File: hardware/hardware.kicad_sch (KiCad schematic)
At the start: 74 parts, among them J1 5025700893, J2 SMA, SW1 PWR switch, U1 BME280, U2 ADS1115IDGS, U3 MS5611-01BA, U4 NEO-M9N, U5 LM2596T-3.3, U6 CC1101RGPR, U7 CC1190RGVT, U8 B39921B3588U410, Y1 26.0 Mhz

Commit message: Updated schematic with better design practices.
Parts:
- removed AE1: W3011, W3011:XDCR_W3011, symbol W3011:W3011
- removed B1: 1079, 1079_KEY, symbol 2026-07-24_00-32-24:1079
- removed C1: 680 uF, symbol Device:C_US
- removed C10, C9: 100pF +- 5%, symbol Device:C_US
- removed C11: 1pF5 +- 0.25%, symbol Device:C_US
- removed C12: 47pF +- 5%, symbol Device:C_US
- removed C13: 0.8pF +- 0.1pF, symbol Device:C_US
- removed C14, C15, C16, C17, C18, C19, C3, C6, C7: 100nF +- 10%, symbol Device:C_US
- removed C2: 330/35 uF/V, symbol Device:C_US
- removed C20: 220 uF, symbol Device:C_US
- removed C21: 10 uF, symbol Device:C_US
- removed C22: 15 pF, symbol Device:C_US
- removed C23: 27 pF, symbol Device:C_US
- removed C24: 1 uF, symbol Device:C_US
- removed C25, C27: 47 pF, symbol Device:C_US
- removed C26: 1 nF, symbol Device:C_US
- removed C28, C29: 12 pF, symbol Device:C_US
- removed C30: 3.3 pF, symbol Device:C_US
- removed C31: 7.5 pF, symbol Device:C_US
- removed C32: DNP, symbol Device:C_US
- removed C33: 1uF, symbol Device:C_US
- removed C4: 12pF +- 5%, symbol Device:C_US
- removed C5: 15pF +- 5%, symbol Device:C_US
- removed C8: 1pF +- .25%, symbol Device:C_US
- removed D0: Red, symbol Device:LED
- removed D1: Blue, symbol Device:LED
- removed D2: 1N5820, Diode_THT:D_DO-201AD_P15.24mm_Horizontal, symbol Diode:1N5820
- removed J1: 5025700893, 502570-0893_MOL, symbol 2026-07-24_01-58-48:5025700893
- removed J2: SMA, symbol Connector:Conn_Coaxial_Small
- removed L10: 7.5 nF, symbol Device:L
- removed L11: 2.9 nF, symbol Device:L
- removed L12: 9.1 nF, symbol Device:L
- removed L13: Bead, symbol Device:L
- removed L3: 12nH +- 5%, symbol Device:L
- removed L4: 18nH +-5%, symbol Device:L
- removed L5: 18nH +- 5&, symbol Device:L
- removed L6: 10nH +-2%, symbol Device:L
- removed L7: 11nH, symbol Device:L
- removed L8: 1.5nH, symbol Device:L
- removed L9: 22nH, symbol Device:L
- removed R1: 10K, symbol Device:R_US
- removed R2, R3: 330, symbol Device:R_US
- removed R4, R5: 33, symbol Device:R_US
- removed R6: 56K, symbol Device:R_US
- removed R7: 3.3K, symbol Device:R_US
- removed R8: 47, symbol Device:R_US
- removed R9: 10, symbol Device:R_US
- removed RT1: PPG102JA, symbol PPG102JA:PPG102JA
- removed SW1: PWR switch, symbol Switch:SW_SPST
- removed U1: BME280, Package_LGA:Bosch_LGA-8_2.5x2.5mm_P0.65mm_ClockwisePinNumbering, symbol Sensor:BME280
- removed U2: ADS1115IDGS, Package_SO:TSSOP-10_3x3mm_P0.5mm, symbol Analog_ADC:ADS1115IDGS
- removed U3: MS5611-01BA, Package_LGA:LGA-8_3x5mm_P1.25mm, symbol Sensor_Pressure:MS5611-01BA
- removed U4: NEO-M9N, RF_GPS:ublox_NEO, symbol RF_GPS:NEO-M9N
- removed U5: LM2596T-3.3, Package_TO_SOT_SMD:TO-263-5_TabPin3, symbol Regulator_Switching:LM2596T-3.3
- removed U6: CC1101RGPR, RGP20_2P4X2P4, symbol 2026-06-04_15-53-20:CC1101RGPR
- removed U7: CC1190RGVT, RGV0016A, symbol 2026-07-24_18-45-18:CC1190RGVT
- removed U8: B39921B3588U410, B39162B3522U410_TDK, symbol 2026-07-24_18-58-53:B39921B3588U410
- removed Y1: 26.0 Mhz, symbol Device:Crystal
- added C1, C30: 1uF, symbol Device:C
- added C101, C132: 15pF, symbol Device:C
- added C111, C141, C151, C181, C41, C51, C91: 100nF, symbol Device:C
- added C121: 1.9pF, symbol Device:C
- added C122, C131: 1.5pF, symbol Device:C
- added C123, C21, C26: 47pF, symbol Device:C
- added C124: 100pF, symbol Device:C
- added C125: 0.8pF, symbol Device:C
- added C161: 27pF, symbol Device:C
- added C2: 10uF, symbol Device:C
- added C22, C52, C81: 12pF, symbol Device:C
- added C24: 3.3pF, symbol Device:C
- added C25: 7.5pF, symbol Device:C
- added C27: 1nF, symbol Device:C
- added C28: DNP, symbol Device:C
- added C3: 220pF, symbol Device:C
- added J1: SMA, symbol Connector:Conn_Coaxial
- added L121, L131: 12nH, symbol Device:L
- added L122, L132: 18nH, symbol Device:L
- added L130: 1.5nH, symbol Device:L
- added L21: 22nH, symbol Device:L
- added L22: 7.5nH, symbol Device:L
- added L23: 2.9nH, symbol Device:L
- added L24: 9.1nH, symbol Device:L
- added L25: 10nH, symbol Device:L
- added P5: BMIS-202, symbol Device:RFShield_TwoPieces
- added R141: 3.3k, symbol Device:R_US
- added R151: 47, symbol Device:R_US
- added R161: 10, symbol Device:R_US
- added R171: 56K, symbol Device:R_US
- added TP1, TP2: TestPoint, symbol Connector:TestPoint
- added U1: CC1101, RGP20_2P4X2P4, symbol 2026-06-04_15-53-20:CC1101RGPR
- added U2: CC1190, RGV0016A, symbol 2026-07-24_18-45-18:CC1190RGVT
- added U3: B39921B3588U410, B39162B3522U410_TDK, symbol 2026-07-24_18-58-53:B39921B3588U410
- added X1: 26.000 MHz, symbol Device:Crystal
- A1: footprint Module:RaspberryPi_Pico_Common_Unspecified -> Module:RaspberryPi_Pico_Common_SMD
- L1: value L32/33 uH -> BEAD
- L2: value 12nH +-5% -> 11nH
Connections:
- net GNDREF: now also A1.33 (AGND), C1.2, C101.2, C111.2, C124.2, C125.2, C131.2, C132.2, C141.2, C151.2, C161.2, C181.2, C2.2, C24.2, C25.2, C26.2, C27.2, C28.2, C3.2, C30.2, C41.2, C51.2, C81.2, C91.2, J1.2 (Ext), P5.1 (Shield), R141.1, R171.2, U1.16 (GND), U1.19 (GND), U1.21 (EPAD), U2.1 (GND), U2.12 (GND), U2.17 (GND), U2.3 (GND), U2.9 (GND), U3.1, U3.3, U3.4, U3.6
- net VDD: now also A1.39 (VSYS), L1.1, L2.2, C3.1
- net at L2.1: now also C161.1, C2.1, C26.1, C27.1, C30.1, L130.1, L21.1, R151.1, R161.1
- net GPS_TX: now reaches A1.1 (GPIO0)
- net LED_GPSF: now reaches A1.10 (GPIO7)
- net SPI1_SCK: now reaches A1.14 (GPIO10)
- net SPI1_SCK: now also U1.1 (SCLK)
- net SPI1_TX: now reaches A1.15 (GPIO11)
- net SPI1_TX: now also U1.20 (SI)
- net SPI1_RX: now reaches A1.16 (GPIO12)
- net SPI1_RX: now also U1.2 (SO)
- net SPI1_CSn: now reaches A1.17 (GPIO13)
- net SPI1_CSn: now also U1.7 (CSN)
- net PA_EN: now reaches A1.19 (GPIO14)
- net PA_EN: now also U2.8 (PA_EN)
- net GPS_RX: now reaches A1.2 (GPIO1)
- net SD_DETECT: now reaches A1.20 (GPIO15)
- net SD_RX: now reaches A1.21 (GPIO16)
- net SD_CSn: now reaches A1.22 (GPIO17)
- net SD_SCK: now reaches A1.24 (GPIO18)
- net SD_TX: now reaches A1.25 (GPIO19)
- net LNA_EN: now reaches A1.26 (GPIO20)
- net LNA_EN: now also U2.7 (LNA_EN)
- net HGM: now reaches A1.27 (GPIO21)
- net HGM: now also U2.6 (HGM)
- net I2C0_SCL: now reaches A1.31 (GPIO26_ADC0)
- net I2C0_SCL: now also A1.7 (GPIO5)
- net I2C0_SDA: now reaches A1.32 (GPIO27_ADC1)
- net I2C0_SDA: now also A1.6 (GPIO4)
- net LED_PWR: now reaches A1.9 (GPIO6)
- net VDD 3V3: no longer names the net of L1.2
- net VDD 3V3: now also C1.1, C111.1, C141.1, C151.1, C181.1, C41.1, C91.1, U1.11 (AVDD), U1.14 (AVDD), U1.15 (AVDD), U1.18 (DGUARD), U1.4 (DVDD), U1.9 (AVDD); no longer A1.37 (3V3_EN)
- new net: C125.1, L25.2, U3.2
- new net: C21.2, L21.2, U2.2 (PA_OUT)
- new net: C21.1, C24.1, L22.1, L23.1
- new net: C25.1, L23.2, L24.1
- new net: C121.1, C122.1, L121.1, L122.2
- new net: L121.2, U1.12 (RF_P)
- new net: C132.1, L130.2, U2.13 (VDD_LNA)
- new net: C22.2, C52.1, U2.4 (TR_SW)
- new net: C52.2, U2.5 (LNA_IN)
- new net: TP2.1, U1.3 (GDO2)
- new net: R161.2, U2.16 (VDD_PA1)
- new net: L25.1, U2.10 (LNA_OUT), U2.11 (PA_IN)
- new net: R151.2, U2.15 (VDD_PA2)
- new net: C101.1, U1.10 (XOSC_Q2), X1.2
- new net: C121.2, C131.1, L131.1, L132.2
- new net: L131.2, U1.13 (RF_N)
- new net: C81.1, U1.8 (XOSC_Q1), X1.1
- new net: C124.1, L122.1
- new net: TP1.1, U1.6 (GDO0)
- new net: R171.1, U1.17 (RBIAS)
- new net: C22.1, L22.2
- new net: C28.1, J1.1 (In), L24.2
- new net: C122.2, C123.1, L132.1
- new net: C123.2, U3.5
- new net: C51.1, U1.5 (DCOUPL)
- new net: R141.2, U2.14 (BIAS)
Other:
- note added: "Goes over U2"
- note removed: "C18-19"
- note removed: "C6-7, C14-17"

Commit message: Added sub pages for different systems.
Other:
- added sheet I2C0 (I2C0.kicad_sch)
- added sheet I2C1_GPS (I2C1_GPS.kicad_sch)
- added sheet SDCard_VDD (SDCard_VDD.kicad_sch)
- moved on the sheet: A1, C1, C101, C111, C121, C122, C123, C124, C125, C131, C132, C141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

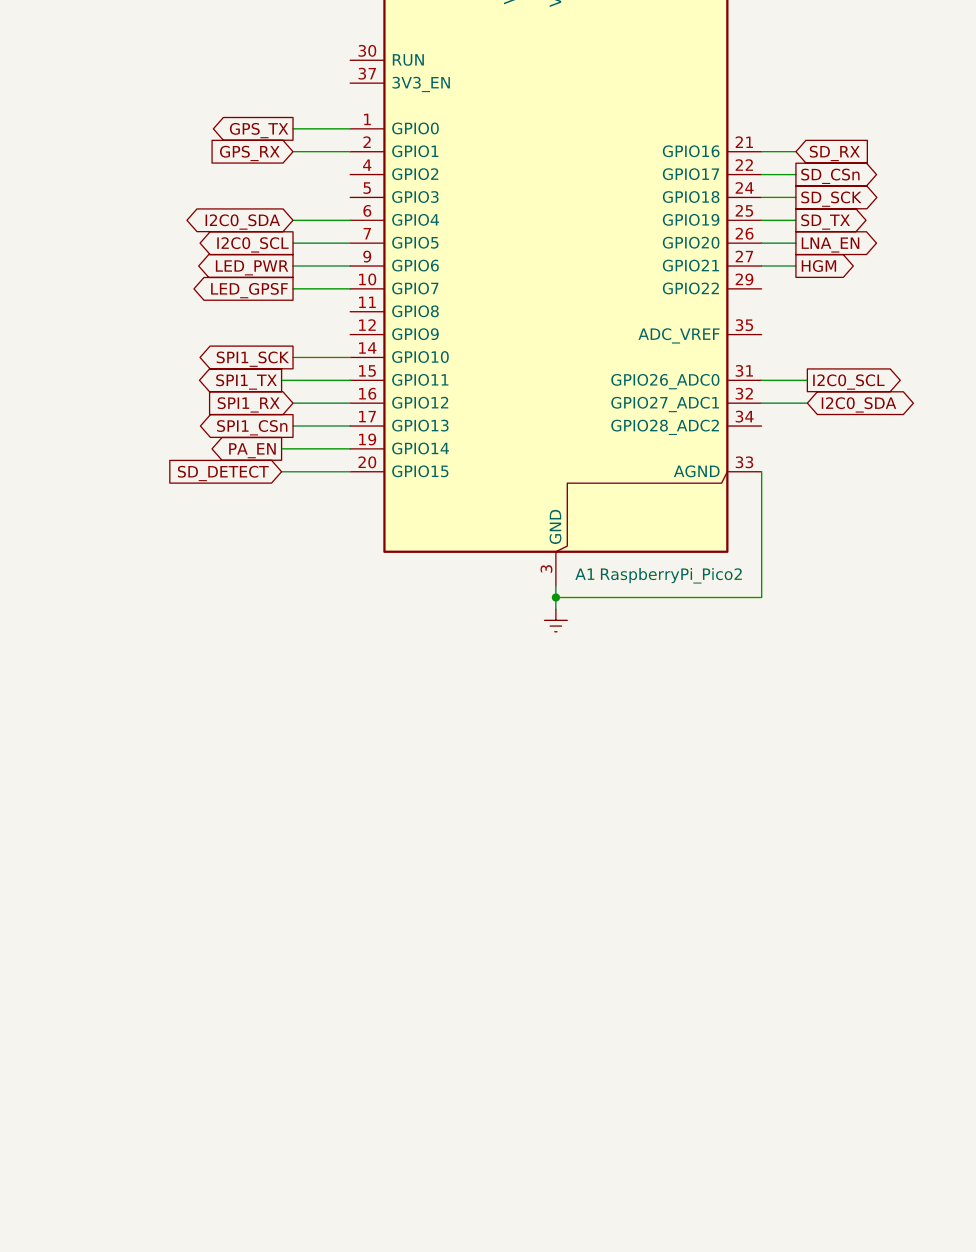
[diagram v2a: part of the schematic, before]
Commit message: More work on the scehmatic for I2C0 and I2C1 + UART GPS.
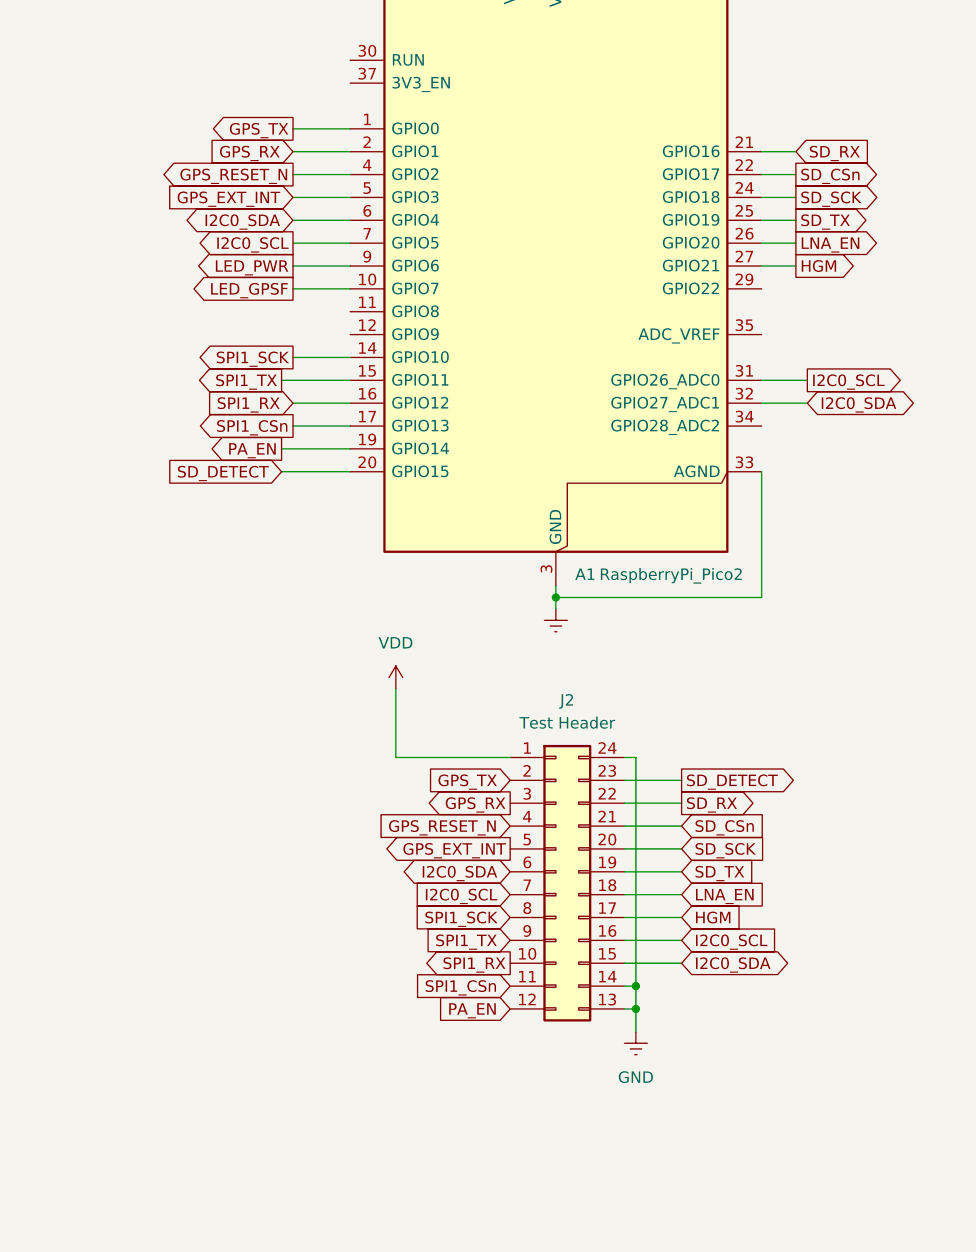
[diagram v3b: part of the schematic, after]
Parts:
- added J2: Test Header, symbol Connector_Generic:Conn_02x12_Counter_Clockwise
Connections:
- net GPS_RX: now also J2.3 (Pin_3)
- net GPS_TX: now also J2.2 (Pin_2)
- net HGM: now also J2.17 (Pin_17)
- net I2C0_SCL: now also J2.16 (Pin_16), J2.7 (Pin_7)
- net I2C0_SDA: now also J2.15 (Pin_15), J2.6 (Pin_6)
- net LNA_EN: now also J2.18 (Pin_18)
- net PA_EN: now also J2.12 (Pin_12)
- net SD_CSn: now also J2.21 (Pin_21)
- net SD_DETECT: now also J2.23 (Pin_23)
- net SD_RX: now also J2.22 (Pin_22)
- net SD_SCK: now also J2.20 (Pin_20)
- net SD_TX: now also J2.19 (Pin_19)
- net SPI1_CSn: now also J2.11 (Pin_11)
- net SPI1_RX: now also J2.10 (Pin_10)
- net SPI1_SCK: now also J2.8 (Pin_8)
- net SPI1_TX: now also J2.9 (Pin_9)
- net VDD: now also J2.1 (Pin_1)
- net GPS_RESET_N: now reaches A1.4 (GPIO2)
- net GPS_RESET_N: now also J2.4 (Pin_4)
- net GPS_EXT_INT: now reaches A1.5 (GPIO3)
- net GPS_EXT_INT: now also J2.5 (Pin_5)
- new net GND: J2.13 (Pin_13), J2.14 (Pin_14), J2.24 (Pin_24)

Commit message: Finished rough draft of the schematic.
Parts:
- removed L1: BEAD, symbol Device:L
- added FB1: FerriteBead, symbol Device:FerriteBead
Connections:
- net GND: now also A1.13 (GND), A1.18 (GND), A1.23 (GND), A1.28 (GND), A1.3 (GND), A1.33 (AGND), A1.38 (GND), A1.8 (GND), C1.2, C101.2, C111.2, C124.2, C125.2, C131.2, C132.2, C141.2, C151.2, C161.2, C181.2, C2.2, C24.2, C25.2, C26.2, C27.2, C28.2, C3.2, C30.2, C41.2, C51.2, C81.2, C91.2, J1.2 (Ext), J2.23 (Pin_23), P5.1 (Shield), R141.1, R171.2, U1.16 (GND), U1.19 (GND), U1.21 (EPAD), U2.12 (GND), U2.17 (GND), U2.9 (GND), U3.1, U3.3, U3.4, U3.6
- net GNDREF: no longer A1.13 (GND), A1.18 (GND), A1.23 (GND), A1.28 (GND), A1.3 (GND), A1.33 (AGND), A1.38 (GND), A1.8 (GND), C1.2, C101.2, C111.2, C124.2, C125.2, C131.2, C132.2, C141.2, C151.2, C161.2, C181.2, C2.2, C24.2, C25.2, C26.2, C27.2, C28.2, C3.2, C30.2, C41.2, C51.2, C81.2, C91.2, J1.2 (Ext), P5.1 (Shield), R141.1, R171.2, U1.16 (GND), U1.19 (GND), U1.21 (EPAD), U2.12 (GND), U2.17 (GND), U2.9 (GND), U3.1, U3.3, U3.4, U3.6
- net SD_DETECT: no longer A1.20 (GPIO15), J2.23 (Pin_23)
- net VDD: now also FB1.2
- net at C1.1, C111.1, C141.1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: now also FB1.1
- no-connect marks 0 -> 8

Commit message: Fixed EEC errors.
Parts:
- added D1: Red LED, symbol Device:LED
- added D2: Blue LED, symbol Device:LED
- added R1, R2: 330, symbol Device:R_US
- U1: footprint RGP20_2P4X2P4 -> Package_DFN_QFN:Texas_RGP0020H_VQFN-20-1EP_4x4mm_P0.5mm_EP2.4x2.4mm_ThermalVias
- U2: footprint RGV0016A -> CC1190RGVT:RGV0016A
- U3: footprint B39162B3522U410_TDK -> B39921B3588U410:B39162B3522U410_TDK-L
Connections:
- net GNDREF is gone; now on net GND: U2.1 (GND), U2.3 (GND)
- net GND: now also D1.1 (K), D2.1 (K); no longer J2.23 (Pin_23)
- net LED_GPSF: now also R2.2
- net LED_PWR: now also R1.2
- net SD_DETECT: now also A1.20 (GPIO15), J2.23 (Pin_23)
- new net: D2.2 (A), R2.1
- new net: D1.2 (A), R1.1
- no-connect marks 8 -> 9

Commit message: Added footprints for the resitors.
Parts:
- P5: value BMIS-202 -> BMIS-202-C
- R1, R2: footprint (none) -> Resistor_SMD:R_1206_3216Metric
- R151, R161, R171: footprint (none) -> Resistor_SMD:R_0402_1005Metric
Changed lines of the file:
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@@
 			)
 		)
-		(property "Footprint" ""
+		(property "Footprint" "Resistor_SMD:R_0402_1005Metric"
 			(at 328.676 86.614 90)
 			(hide yes)
@@
 			)
 		)
-		(property "Footprint" ""
+		(property "Footprint" "Resistor_SMD:R_0402_1005Metric"
 			(at 323.596 86.614 90)
 			(hide yes)
@@
 			)
 		)
-		(property "Footprint" ""
+		(property "Footprint" "Resistor_SMD:R_0402_1005Metric"
 			(at 253.746 175.514 90)
 			(hide yes)
@@
 			)
 		)
-		(property "Footprint" ""
+		(property "Footprint" "Resistor_SMD:R_1206_3216Metric"
 			(at 157.226 31.496 90)
 			(hide yes)
@@
 			)
 		)
-		(property "Footprint" ""
+		(property "Footprint" "Resistor_SMD:R_1206_3216Metric"
 			(at 157.226 21.336 90)
 			(hide yes)
@@
 			)
 		)
-		(property "Value" "BMIS-202"
+		(property "Value" "BMIS-202-C"
 			(at 307.34 167.0049 0)
 			(show_name no)
@@
 			)
 		)
-		(property "Description" "Two-piece EMI RF shielding cabinet"
+		(property "Description" "Snap fit"
 			(at 288.29 167.64 0)
 			(hide yes)

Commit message: Added capacitor footprints.
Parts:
- C1, C101, C111, C121, C122, C123, C124, C125, C131, C132, C141, C151, C161, C181, C2, C21, C22, C24, C25, C26, C27, C28, C3, C30, C41, C51, C52, C81, C91: footprint (none) -> Capacitor_SMD:C_0402_1005Metric
- D1, D2: footprint (none) -> LED_THT:LED_D5.0mm
- J2: footprint (none) -> Connector_PinSocket_2.54mm:PinSocket_2x12_P2.54mm_Vertical
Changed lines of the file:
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@@
 			)
 		)
-		(property "Footprint" ""
+		(property "Footprint" "Capacitor_SMD:C_0402_1005Metric"
 			(at 310.8452 120.65 0)
 			(hide yes)
@@
 			)
 		)
-		(property "Footprint" ""
+		(property "Footprint" "Capacitor_SMD:C_0402_1005Metric"
 			(at 210.5152 179.07 0)
 			(hide yes)
@@
 			)
 		)
-		(property "Footprint" ""
+		(property "Footprint" "Capacitor_SMD:C_0402_1005Metric"
 			(at 299.4152 88.9 0)
 			(hide yes)
@@
 			)
 		)
-		(property "Footprint" ""
+		(property "Footprint" "Capacitor_SMD:C_0402_1005Metric"
 			(at 396.24 151.4348 0)
 			(hide yes)
@@
 			)
 		)
-		(property "Footprint" ""
+		(property "Footprint" "Capacitor_SMD:C_0402_1005Metric"
 			(at 312.1152 88.9 0)
 			(hide yes)
@@
 			)
 		)
-		(property "Footprint" ""
+		(property "Footprint" "Capacitor_SMD:C_0402_1005Metric"
 			(at 378.46 127.3048 0)
 			(hide yes)
@@
 			)
 		)
-		(property "Footprint" ""
+		(property "Footprint" "Capacitor_SMD:C_0402_1005Metric"
 			(at 221.9452 179.07 0)
 			(hide yes)
@@
 			)
 		)
-		(property "Footprint" ""
+		(property "Footprint" "Capacitor_SMD:C_0402_1005Metric"
 			(at 244.8052 179.07 0)
 			(hide yes)
@@
 			)
 		)
-		(property "Footprint" ""
+		(property "Footprint" "Capacitor_SMD:C_0402_1005Metric"
 			(at 131.7752 149.86 0)
 			(hide yes)
@@
 			)
 		)
-		(property "Footprint" ""
+		(property "Footprint" "Capacitor_SMD:C_0402_1005Metric"
 			(at 389.5852 82.55 0)
 			(hide yes)
@@
 			)
 		)
-		(property "Footprint" ""
+		(property "Footprint" "LED_THT:LED_D5.0mm"
 			(at 165.1 30.48 0)
 			(hide yes)
@@
 			)
 		)
-		(property "Footprint" ""
+		(property "Footprint" "Capacitor_SMD:C_0402_1005Metric"
 			(at 228.2952 116.84 0)
 			(hide yes)
@@
 			)
 		)
-		(property "Footprint" ""
+		(property "Footprint" "Capacitor_SMD:C_0402_1005Metric"
 			(at 287.9852 88.9 0)
 			(hide yes)
@@
 			)
 		)
-		(property "Footprint" ""
+		(property "Footprint" "Capacitor_SMD:C_0402_1005Metric"
 			(at 397.2052 82.55 0)
 			(hide yes)
@@
 			)
 		)
-		(property "Footprint" ""
+		(property "Footprint" "LED_THT:LED_D5.0mm"
 			(at 165.1 20.32 0)
 			(hide yes)
@@
 			)
 		)
-		(property "Footprint" ""
+		(property "Footprint" "Capacitor_SMD:C_0402_1005Metric"
 			(at 228.2952 124.46 0)
 			(hide yes)
@@
 			)
 		)
-		(property "Footprint" ""
+		(property "Footprint" "Capacitor_SMD:C_0402_1005Metric"
 			(at 334.9752 149.86 0)
 			(hide yes)
@@
 			)
 		)
-		(property "Footprint" ""
+		(property "Footprint" "Capacitor_SMD:C_0402_1005Metric"
 			(at 257.81 112.0648 0)
 			(hide yes)
@@
 			)
 		)
-		(property "Footprint" ""
+		(property "Footprint" "Capacitor_SMD:C_0402_1005Metric"
 			(at 144.4752 152.4 0)
 			(hide yes)
@@
 			)
 		)
-		(property "Footprint" ""
+		(property "Footprint" "Capacitor_SMD:C_0402_1005Metric"
 			(at 154.6352 179.07 0)
 			(hide yes)
@@
 			)
 		)
-		(property "Footprint" ""
+		(property "Footprint" "Capacitor_SMD:C_0402_1005Metric"
 			(at 275.2852 88.9 0)
 			(hide yes)
@@
 			)
 		)
-		(property "Footprint" ""
+		(property "Footprint" "Capacitor_SMD:C_0402_1005Metric"
 			(at 241.3 108.2548 0)
 			(hide yes)
@@
 			)
 		)
-		(property "Footprint" ""
+		(property "Footprint" "Capacitor_SMD:C_0402_1005Metric"
 			(at 365.4552 149.86 0)
 			(hide yes)
@@
 			)
 		)
-		(property "Footprint" ""
+		(property "Footprint" "Capacitor_SMD:C_0402_1005Metric"
 			(at 345.1352 149.86 0)
 			(hide yes)
@@
 			)
 		)
-		(property "Footprint" ""
+		(property "Footprint" "Capacitor_SMD:C_0402_1005Metric"
 			(at 355.2952 149.86 0)
 			(hide yes)
@@
 			)
 		)
-		(property "Footprint" ""
+		(property "Footprint" "Capacitor_SMD:C_0402_1005Metric"
 			(at 113.9952 214.63 0)
 			(hide yes)
@@
 			)
 		)
-		(property "Footprint" ""
+		(property "Footprint" "Capacitor_SMD:C_0402_1005Metric"
 			(at 404.8252 82.55 0)
 			(hide yes)
@@
 			)
 		)
-		(property "Footprint" ""
+		(property "Footprint" "Capacitor_SMD:C_0402_1005Metric"
 			(at 233.3752 179.07 0)
 			(hide yes)
@@
 			)
 		)
-		(property "Footprint" ""
+		(property "Footprint" "Capacitor_SMD:C_0402_1005Metric"
 			(at 144.4752 179.07 0)
 			(hide yes)
@@
 			)
 		)
-		(property "Footprint" ""
+		(property "Footprint" "Capacitor_SMD:C_0402_1005Metric"
 			(at 241.3 86.6648 0)
 			(hide yes)
@@
 			)
 		)
-		(property "Footprint" ""
+		(property "Footprint" "Capacitor_SMD:C_0402_1005Metric"
 			(at 113.9952 149.86 0)
 			(hide yes)
@@
 			)
 		)
-		(property "Footprint" ""
+		(property "Footprint" "Connector_PinSocket_2.54mm:PinSocket_2x12_P2.54mm_Vertical"
 			(at 59.69 127 0)
 			(hide yes)
